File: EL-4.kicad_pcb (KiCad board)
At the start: 2 copper layers, 31 x 18.5 mm, 17 parts, among them J1 Conn_01x02, J2 Conn_01x03, Q1 BSS214NW, Q2 BSS214NW, U1 MIC4832

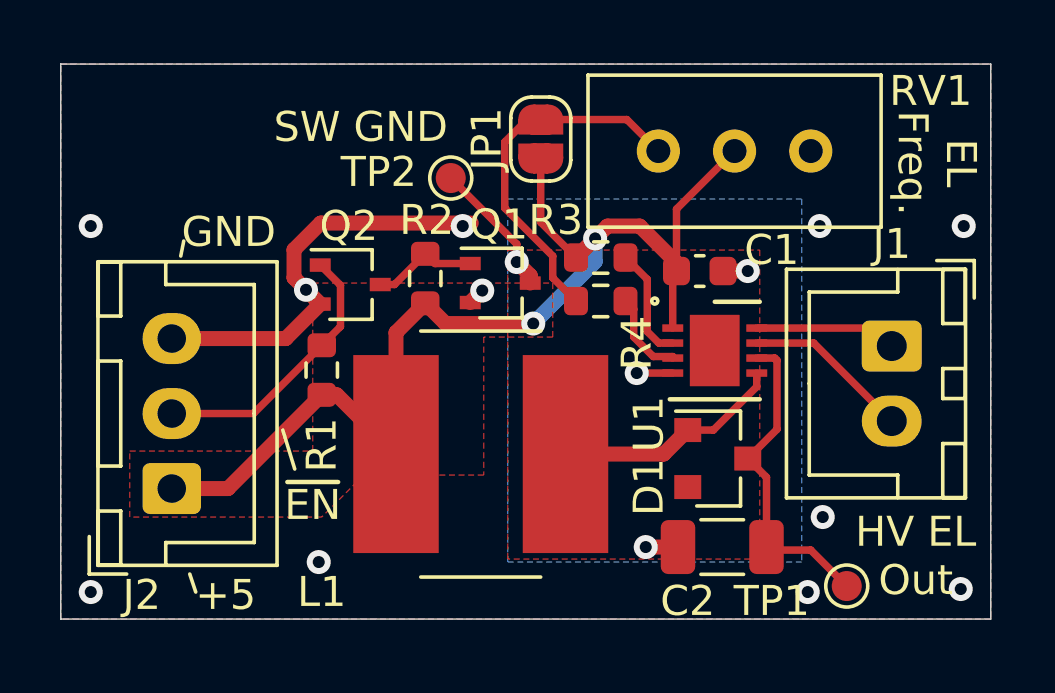
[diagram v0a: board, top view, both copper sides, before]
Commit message: Version 1.0.
Changed enable method to pull RSW R3 to ground.
Changed R3, R4, R5 and C2 for 100Hz operation for 3 square inches.
Added input filter cap.

Also added BOM.

Signed-off-by: Aaron Williams <aaron.w2@gmail.com>
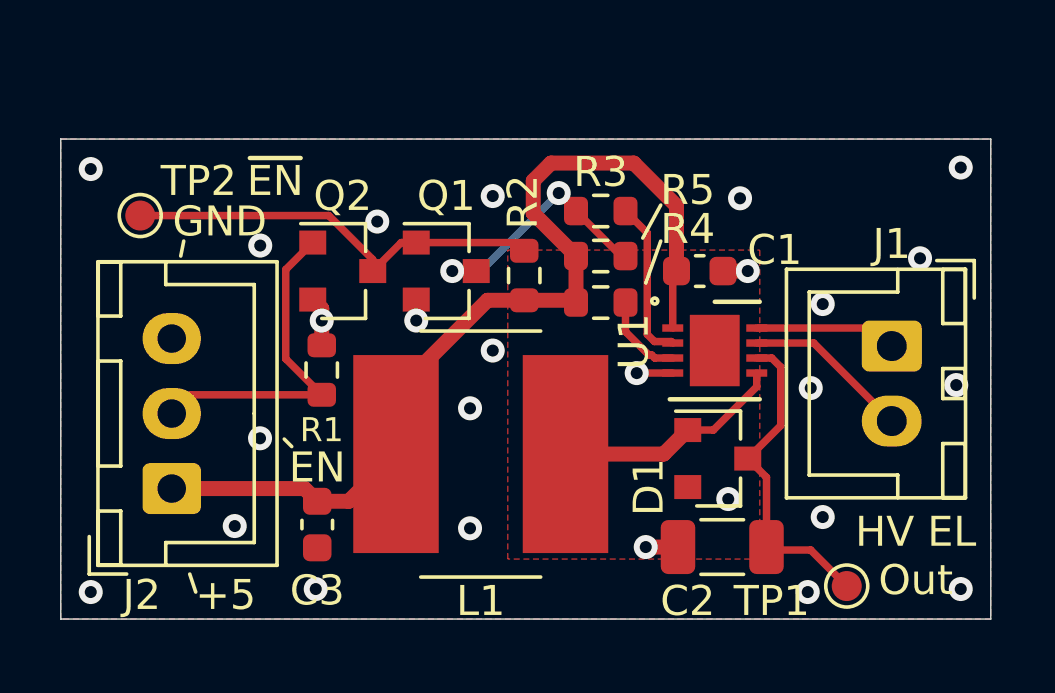
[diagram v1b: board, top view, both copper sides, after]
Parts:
- removed JP1: Jumper_NO_Small, Jumper:SolderJumper-2_P1.3mm_Open_RoundedPad1.0x1.5mm
- removed RV1: 1.2M, Potentiometer_THT:Potentiometer_Bourns_3296W_Vertical
- added C3: 10uF, Capacitor_SMD:C_0603_1608Metric, F.Cu at (77.5, 60.9)
- added R5: 1K, Resistor_SMD:R_0603_1608Metric, F.Cu at (87.0, 51.9)
- added REF**: Symbol_HighVoltage_Type2_SilkscreenTop_VerySmall, Aaron:Symbol_HighVoltage_Type2_SilkscreenTop_VerySmall, B.Cu at (89.8, 52.6)
- added REF**: Symbol_CC-Noncommercial_CopperTop_Small, Aaron:Symbol_CC-Noncommercial_SilkscreenTop_Small, B.Cu at (75.5, 50.9)
- C2: value 0.01uF 250V -> 0.015uF 250V
- Q1, Q2: value BSS214NW -> BSS138; footprint Package_TO_SOT_SMD:SOT-323_SC-70 -> Package_TO_SOT_SMD:SOT-23
- R3: value 332K -> 309K
- R4: value 360K -> 1.69M
- TP2: value TestPoint_Small -> TestPoint
- moved TP2 10.4 mm to (71.7, 50.5)
- moved R2 3.30 mm to (84.5, 52.5)
- moved Q1 1.84 mm to (81.8, 52.4)
- moved R3 1.55 mm to (87.0, 50.4)
- moved Q2 0.51 mm to (78.4, 52.4)
- moved R4 0.05 mm to (87.0, 53.5)
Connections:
- C1 pad 2: /SW_GND -> GND
- C2 pad 2: /SW_GND -> GND
- J2 pad 2: /~EN -> /EN
- Q1 pad 1: /EN -> /~EN
- Q1 pad 3: /SW_GND -> Net-(Q1-Pad3)
- Q2 pad 1: /~EN -> /EN
- Q2 pad 3: /EN -> /~EN
- R1 pad 1: /~EN -> GND
- R1 pad 2: +5V -> /EN
- R2 pad 1: /EN -> /~EN
- R3 pad 2: +5V -> Net-(Q1-Pad3)
- R4 pad 2: Net-(JP1-Pad2) -> +5V
- TP2 pad 1: /SW_GND -> /~EN
- U1 pad 4: /SW_GND -> GND
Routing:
- net Net-(JP1-Pad2): track 12.1 -> 0.00 mm
- net GND: track 14.4 -> 4.75 mm, vias 11 -> 26
- net Net-(Q1-Pad3): track 0.00 -> 8.54 mm, vias 0 -> 2
- net /SW_GND: track 7.70 -> 0.00 mm, vias 4 -> 0
- net /EN: track 3.56 -> 11.2 mm
- net /~EN: track 9.16 -> 14.3 mm
- net +5V: track 37.7 -> 34.3 mm, vias 2 -> 0
- net Net-(R3-Pad1): track 3.77 -> 5.38 mm
- removed copper zone on F.Cu, net +5V
- removed copper zone on B.Cu, net /SW_GND
- removed copper zone on F.Cu, net /SW_GND
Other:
- board size 31 x 18.5 mm -> 31 x 16 mm
- board text added: "EN"
- board text added: "GND EN +5"
- board text added: "TP2: ~EN~"
- board text added: "Version 1.0"
- board text removed: "EL Freq."
- board text removed: "GND ~EN~ +5"
- board text removed: "SW GND"
- board text removed: "Short JP1 for 1KHz"
- board text removed: "TP2: Switched GND"
- board text removed: "Turn trim pot adjust EL frequency"
- board text removed: "Version 0.9"
